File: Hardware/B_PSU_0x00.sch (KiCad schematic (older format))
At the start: 113 parts, among them J1 Conn_01x03, J10 Conn_01x02, J11 Conn_01x02, J12 Conn_01x02, J13 Conn_01x02, J14 Conn_01x02, J15 Conn_01x02, J16 Conn_01x03, J17 Conn_01x02, J2 Conn_01x02, J3 Conn_01x02, J4 Conn_01x02, J5 Conn_01x02, J6 Conn_01x02, J7 Conn_01x03, J8 Conn_01x02, J9 Conn_01x03, U1 ADP5070AREZ, U2 ADP7142AUJZ, U3 ADP7182AUJZ, U5 ADP7142AUJZ, U7 ADP7182AUJZ, U8 ADP5070AREZ

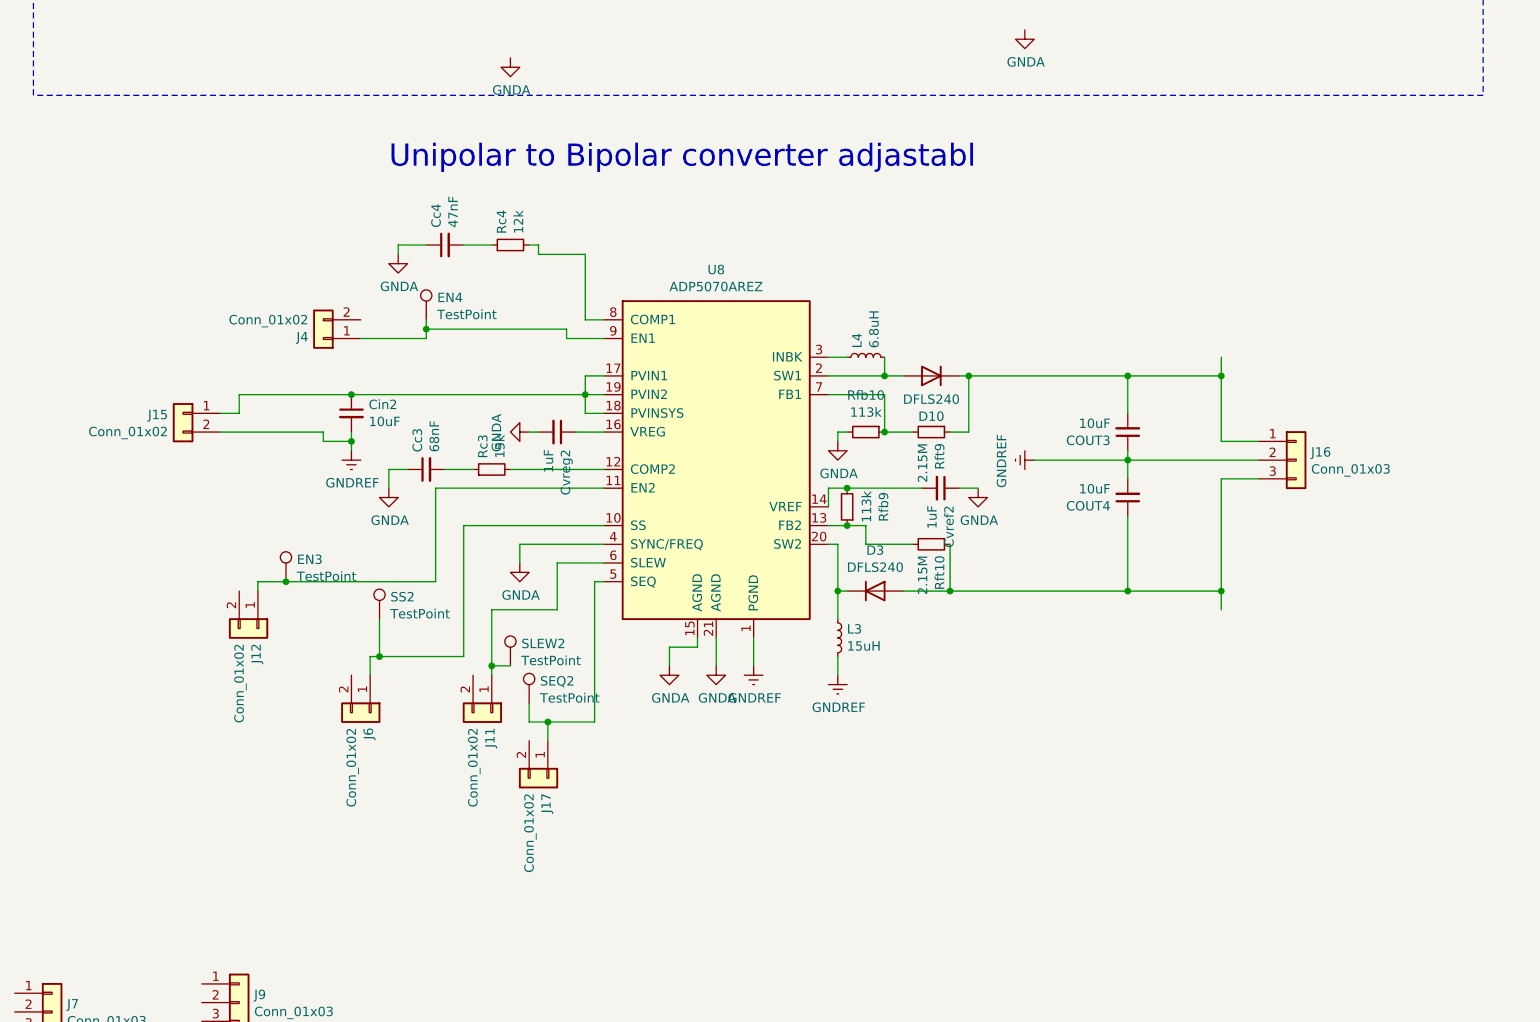
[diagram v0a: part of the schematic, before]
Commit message: Update B_PSU_0x00.sch
Changed number of ADP5070 converters from two to one
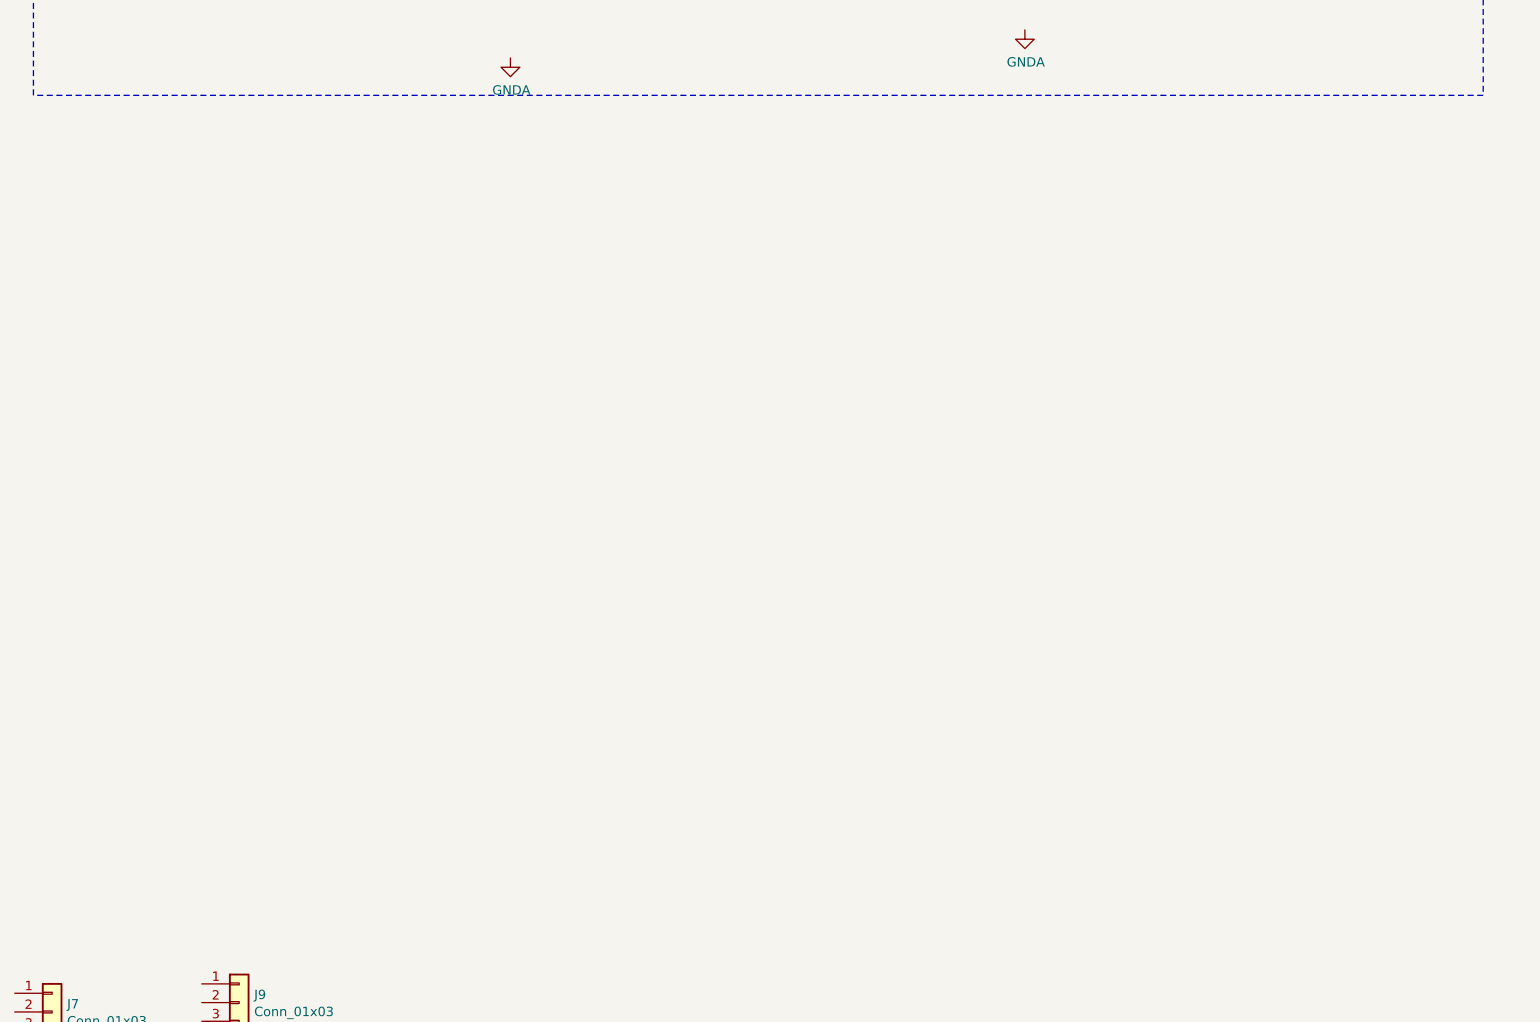
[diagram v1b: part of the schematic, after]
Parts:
- removed COUT3, COUT4: 10uF, Capacitor_SMD:C_1210_3225Metric_Pad1.33x2.70mm_HandSolder, symbol Device:C_Small
- removed Cc3: 68nF, Capacitor_SMD:C_0805_2012Metric_Pad1.18x1.45mm_HandSolder, symbol Device:C_Small
- removed Cc4: 47nF, Capacitor_SMD:C_0805_2012Metric_Pad1.18x1.45mm_HandSolder, symbol Device:C_Small
- removed Cin2: 10uF, Capacitor_SMD:C_1206_3216Metric_Pad1.33x1.80mm_HandSolder, symbol Device:C_Small
- removed Cvref2, Cvreg2: 1uF, Capacitor_SMD:C_0805_2012Metric_Pad1.18x1.45mm_HandSolder, symbol Device:C_Small
- removed D10, D3: DFLS240, Diode_SMD:D_SOD-123F, symbol Device:D
- removed EN3, EN4, SEQ2, SLEW2, SS2: TestPoint, symbol Connector:TestPoint
- removed J11, J12, J17, J4, J6: Conn_01x02, Connector_PinHeader_2.54mm:PinHeader_1x02_P2.54mm_Vertical, symbol Connector_Generic:Conn_01x02
- removed J15: Conn_01x02, TerminalBlock:TerminalBlock_bornier-2_P5.08mm, symbol Connector_Generic:Conn_01x02
- removed J16: Conn_01x03, TerminalBlock:TerminalBlock_bornier-3_P5.08mm, symbol Connector_Generic:Conn_01x03
- removed L3: 15uH, Inductor_SMD:L_Coilcraft_XxL4030, symbol Device:L_Small
- removed L4: 6.8uH, Inductor_SMD:L_Coilcraft_XxL4040, symbol Device:L_Small
- removed Rc3: 15k, Resistor_SMD:R_0805_2012Metric_Pad1.20x1.40mm_HandSolder, symbol Device:R_Small
- removed Rc4: 12k, Resistor_SMD:R_0805_2012Metric_Pad1.20x1.40mm_HandSolder, symbol Device:R_Small
- removed Rfb10, Rfb9: 113k, Resistor_SMD:R_0805_2012Metric_Pad1.20x1.40mm_HandSolder, symbol Device:R_Small
- removed Rft10, Rft9: 2.15M, Resistor_SMD:R_0805_2012Metric_Pad1.20x1.40mm_HandSolder, symbol Device:R_Small
- removed U8: ADP5070AREZ, Package_SO:ETSSOP-20-1EP_4.4x6.5mm_P0.65mm_EP3x4.2mm, symbol Regulator_Switching:ADP5070AREZ
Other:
- note removed: "Unipolar to Bipolar converter adjastabl\n"

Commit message: LDO's changed to the ones you can buy
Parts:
- removed Cnr3, Cnr4, Cnr5, Cnr6: 1uF, Capacitor_SMD:C_0805_2012Metric_Pad1.18x1.45mm_HandSolder, symbol Device:C_Small
- removed H3, H6: MountingHole, MountingHole:MountingHole_3.2mm_M3, symbol Mechanical:MountingHole
- removed J2, J3: Conn_01x02, TerminalBlock:TerminalBlock_bornier-2_P5.08mm, symbol Connector_Generic:Conn_01x02
- removed Rfb3, Rfb4, Rfb5, Rfb6: 10k, Resistor_SMD:R_0805_2012Metric_Pad1.20x1.40mm_HandSolder, symbol Device:R_Small
- removed Rft3, Rft4, Rft5, Rft6: 20k, Resistor_SMD:R_0805_2012Metric_Pad1.20x1.40mm_HandSolder, symbol Device:R_Small
- removed Rnr3, Rnr4, Rnr5, Rnr6: 1k, Resistor_SMD:R_0805_2012Metric_Pad1.20x1.40mm_HandSolder, symbol Device:R_Small
- removed U2, U5: ADP7142AUJZ, Package_TO_SOT_SMD:TSOT-23-5, symbol Regulator_Linear:ADP7142AUJZ
- removed U3, U7: ADP7182AUJZ, Package_TO_SOT_SMD:TSOT-23-5, symbol Regulator_Linear:ADP7182AUJZ
- added Cin2, Cin7, Cin8, Cin9: 10uF, Capacitor_SMD:C_1206_3216Metric_Pad1.33x1.80mm_HandSolder, symbol Device:C_Small
- added Cout1, Cout2, Cout7, Cout8: 2.2uF, Capacitor_SMD:C_1206_3216Metric_Pad1.33x1.80mm_HandSolder, symbol Device:C_Small
- added D10, D3, D5, D6: LED, LED_SMD:LED_PLCC-2, symbol Device:LED
- added J11, J12, J4, J6: Conn_01x02, TerminalBlock:TerminalBlock_bornier-2_P5.08mm, symbol Connector_Generic:Conn_01x02
- added J15, J16, J17: Conn_01x03, Connector_PinHeader_2.54mm:PinHeader_1x03_P2.54mm_Vertical, symbol Connector_Generic:Conn_01x03
- added J18, J19, J2, J3: Conn_01x04, Connector_PinHeader_2.54mm:PinHeader_1x04_P2.54mm_Vertical, symbol Connector_Generic:Conn_01x04
- added R1, R3, R4, R8, Rbr10, Rbr13, Rbr14, Rbr15, Rbr16, Rbr5, Rbr6, Rbr9: 0R, Resistor_SMD:R_0805_2012Metric_Pad1.20x1.40mm_HandSolder, symbol Device:R_Small
- added U2: ADP7142AUJZ-5.0, Package_TO_SOT_SMD:TSOT-23-5, symbol Regulator_Linear:ADP7142AUJZ-5.0
- added U3: ADP7142AUJZ-3.3, Package_TO_SOT_SMD:TSOT-23-5, symbol Regulator_Linear:ADP7142AUJZ-3.3
- added U4: ADP7142AUJZ-1.8, Package_TO_SOT_SMD:TSOT-23-5, symbol Regulator_Linear:ADP7142AUJZ-1.8
- added U5: ADP7182AUJZ-1.8, Package_TO_SOT_SMD:TSOT-23-5, symbol Regulator_Linear:ADP7182AUJZ-1.8
- added U6: ADP7142AUJZ-2.5, Package_TO_SOT_SMD:TSOT-23-5, symbol Regulator_Linear:ADP7142AUJZ-2.5
- added U7: ADP7183ACPZN3.3-R7, SON50P200X200X60-9N, symbol SAE_spec:ADP7183ACPZN3.3-R7
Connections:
- wire segments 281 -> 355
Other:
- moved on the sheet: Cin5, Cout3, D8, H1, H2, H4, H5, J9, R6, Rbr7, Rbr8

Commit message: updated to sch and pcb
correct LDO ic's and board outline
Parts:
- removed H5: MountingHole, MountingHole:MountingHole_3.2mm_M3, symbol Mechanical:MountingHole
- removed J10, J8: Conn_01x02, Connector_PinHeader_2.54mm:PinHeader_1x02_P2.54mm_Vertical, symbol Connector_Generic:Conn_01x02
- removed J11, J12, J13, J4, J5, J6: Conn_01x02, TerminalBlock:TerminalBlock_bornier-2_P5.08mm, symbol Connector_Generic:Conn_01x02
- removed J15, J16, J17, J7, J9: Conn_01x03, Connector_PinHeader_2.54mm:PinHeader_1x03_P2.54mm_Vertical, symbol Connector_Generic:Conn_01x03
- removed J18, J19, J2, J3: Conn_01x04, Connector_PinHeader_2.54mm:PinHeader_1x04_P2.54mm_Vertical, symbol Connector_Generic:Conn_01x04
- removed U2: ADP7142AUJZ-5.0, Package_TO_SOT_SMD:TSOT-23-5, symbol Regulator_Linear:ADP7142AUJZ-5.0
- removed U3: ADP7142AUJZ-3.3, Package_TO_SOT_SMD:TSOT-23-5, symbol Regulator_Linear:ADP7142AUJZ-3.3
- removed U5: ADP7182AUJZ-1.8, Package_TO_SOT_SMD:TSOT-23-5, symbol Regulator_Linear:ADP7182AUJZ-1.8
- removed U6: ADP7142AUJZ-2.5, Package_TO_SOT_SMD:TSOT-23-5, symbol Regulator_Linear:ADP7142AUJZ-2.5
- added H3: MountingHole, MountingHole:MountingHole_3.2mm_M3, symbol Mechanical:MountingHole
- added J11, J12, J13, J18, J19, J20, J21, J22, J3, J4, J5, J6: Conn_01x03, Connector_PinHeader_2.54mm:PinHeader_1x03_P2.54mm_Vertical, symbol Connector_Generic:Conn_01x03
- added SW1, SW2, SW3, SW4: SW_DPDT_x2, Connector_PinHeader_2.54mm:PinHeader_2x03_P2.54mm_Vertical, symbol Switch:SW_DPDT_x2
- added U2: ADP7118WAUJZ-5.0, Package_TO_SOT_SMD:TSOT-23-5_HandSoldering, symbol SAE_spec:ADP7118WAUJZ-5.0
- added U3: ADP7118AUJZ-3.3-R7, Package_TO_SOT_SMD:TSOT-23-5_HandSoldering, symbol SAE_spec:ADP7118AUJZ-3.3-R7
- added U5: ADP7118AUJZ-2.5-R7, Package_TO_SOT_SMD:TSOT-23-5_HandSoldering, symbol SAE_spec:ADP7118AUJZ-2.5-R7
- added U6: ADP7182ACPZ-5.0-R7, Package_CSP:LFCSP-8-1EP_3x3mm_P0.5mm_EP1.45x1.74mm, symbol SAE_spec:ADP7182ACPZ-5.0-R7
- added U8: ADP7182ACPZN-2.5R7, Package_DFN_QFN:DFN-6-1EP_2x2mm_P0.65mm_EP1x1.6mm, symbol SAE_spec:ADP7182ACPZN-2.5R7
- added U9: ADP7182AUJZ-1.8, Package_TO_SOT_SMD:TSOT-23-5, symbol Regulator_Linear:ADP7182AUJZ-1.8
- Cin4: value 10uF -> 4.7uF
- Cout4: value 2.2uF -> 4.7uF
- EN1, EN2, SEQ1, SLEW1, SS1: footprint (none) -> TestPoint:TestPoint_Pad_D2.5mm
- U4: footprint Package_TO_SOT_SMD:TSOT-23-5 -> Package_TO_SOT_SMD:TSOT-23-5_HandSoldering
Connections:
- net labels added: +1v8, +2v5, +3v3, +5V, -1v8, -2v5, -3v3, -5V, EN_+1v8, EN_+2v5, EN_+3v3, EN_+5v, EN_-1v8, EN_-2v5, EN_-3v3, EN_-5v
- wire segments 355 -> 479
- no-connect marks 0 -> 4
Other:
- note added: "+/- 1v8 LDO\n"
- note added: "+/- 5v0 LDO\n"
- moved on the sheet: Cin9, Cout1, Rbr15, Rbr16

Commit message: WIP
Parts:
- removed D10, D4, D5, D6, D7, D8, D9: LED, LED_SMD:LED_PLCC-2, symbol Device:LED
- removed R2, R3, R4, R5, R6, R7, R8, Rbr1, Rbr10, Rbr11, Rbr12, Rbr13, Rbr14, Rbr15, Rbr16, Rbr2, Rbr3, Rbr4, Rbr5, Rbr6, Rbr7, Rbr8, Rbr9: 0R, Resistor_SMD:R_0805_2012Metric_Pad1.20x1.40mm_HandSolder, symbol Device:R_Small
- added J10, J15, J16, J17, J2, J23, J24, J25, J26, J7, J8, J9: Conn_01x02, Connector_PinHeader_2.54mm:PinHeader_1x02_P2.54mm_Vertical, symbol Connector_Generic:Conn_01x02
- added J27, J28: Conn_01x03, Connector_PinHeader_2.54mm:PinHeader_1x03_P2.54mm_Vertical, symbol Connector_Generic:Conn_01x03
- J1: footprint TerminalBlock:TerminalBlock_bornier-3_P5.08mm -> Connector_PinHeader_2.54mm:PinHeader_1x03_P2.54mm_Vertical
- SW1, SW2, SW3, SW4: footprint Connector_PinHeader_2.54mm:PinHeader_2x03_P2.54mm_Vertical -> Connector_PinHeader_2.54mm:PinHeader_1x06_P2.54mm_Vertical
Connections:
- net EN_+3v3: now also SW4.2 (B); no longer SW2.5 (B)
- net EN_-1v8: now also SW2.5 (B); no longer SW4.2 (B)
- net EN_-2v5: now also SW3.5 (B); no longer SW4.5 (B)
- net EN_-3v3: now also SW4.5 (B); no longer SW3.5 (B)
- net GNDA: now also J27.2 (Pin_2), J28.2 (Pin_2); no longer Cin2.2, Cin3.2, Cin4.2, Cin5.2, Cin6.2, Cin7.1, Cin8.2, Cin9.1, Cout3.2, Cout4.1, Cout5.2, Cout6.1, Cout7.2, Cout8.1, D3.1 (K), J11.2 (Pin_2), J12.2 (Pin_2), J13.2 (Pin_2), J18.2 (Pin_2), J19.2 (Pin_2), J21.2 (Pin_2), J22.2 (Pin_2), J3.2 (Pin_2), J5.2 (Pin_2), U2.2 (GND), U3.2 (GND), U4.2 (GND), U5.2 (GND), U6.6 (GND), U7.6 (GND), U8.5 (GND), U9.1 (GND)
- net Vneg: now also J27.3 (Pin_3), J28.3 (Pin_3)
- net Vpoz: now also J27.1 (Pin_1), J28.1 (Pin_1)
- net at Cin3.1, U3.1 (Vin): now also J9.2 (Pin_2)
- net at Cin4.1, U7.8 (VIN), U7.9 (EXP): now also J10.2 (Pin_2)
- net at Cin5.1, U5.1 (Vin): now also J17.2 (Pin_2)
- net at Cin6.1, U8.6 (Vin), U8.7 (EP): now also J15.2 (Pin_2)
- net at Cin2.1, U2.1 (Vin): now also J7.2 (Pin_2); no longer R1.1
- net at Cin8.1, U4.1 (VIN): now also J16.2 (Pin_2)
- net at Cout1.1, Cout2.2, J20.2 (Pin_2)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: now also Cin2.2, Cin7.1, U2.2 (GND), U6.6 (GND), J23.2 (Pin_2)
- net at Cin9.2, U9.2 (VIN): now also J8.2 (Pin_2)
- net at Cin7.2, U6.7 (Vin), U6.8 (Vin)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: now also J2.2 (Pin_2)
- new net: Cin3.2, Cin4.2, Cout3.2, Cout4.1, J12.2 (Pin_2), J19.2 (Pin_2), J25.2 (Pin_2), J3.2 (Pin_2), U3.2 (GND), U7.6 (GND)
- new net: Cin5.2, Cin6.2, Cout5.2, Cout6.1, J11.2 (Pin_2), J18.2 (Pin_2), J22.2 (Pin_2), J26.2 (Pin_2), U5.2 (GND), U8.5 (GND)
- new net: Cin8.2, Cin9.1, Cout7.2, Cout8.1, J13.2 (Pin_2), J21.2 (Pin_2), J24.2 (Pin_2), J5.2 (Pin_2), U4.2 (GND), U9.1 (GND)
- new net GND_1v8: J24.1 (Pin_1)
- new net GND_2v5: J26.1 (Pin_1)
- new net GND_3v3: J25.1 (Pin_1)
- new net GND_5v: J23.1 (Pin_1)
- new net Vin_+1v8: J16.1 (Pin_1)
- new net Vin_+2v5: J17.1 (Pin_1)
- new net Vin_+3v3: J9.1 (Pin_1)
- new net Vin_+5v: J7.1 (Pin_1)
- new net Vin_-1v8: J8.1 (Pin_1)
- new net Vin_-2v5: J15.1 (Pin_1)
- new net Vin_-3v3: J10.1 (Pin_1)
- new net Vin_-5v: J2.1 (Pin_1)
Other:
- moved on the sheet: SW2A, SW2B, SW3B, SW4A, SW4B
